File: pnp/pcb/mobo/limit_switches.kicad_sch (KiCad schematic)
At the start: 6 parts, among them J2 X_LIMIT, J3 Y_LIMIT, J4 Z_LIMIT, J5 L_LIMIT, J6 R_LIMIT, J7 A_LIMIT

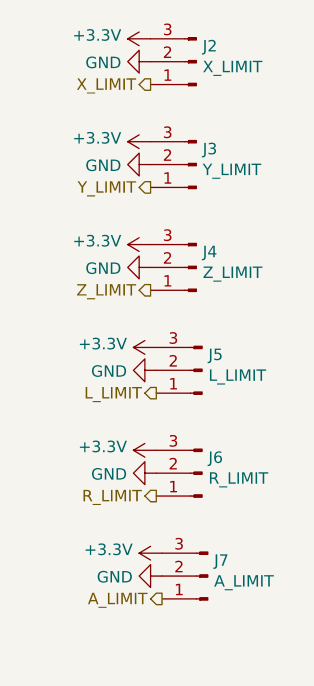
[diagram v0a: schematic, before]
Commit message: All sheets cleaned up
All symbols and their fields are now neatly organized.

All hierarchical pins are already imported,
except for the microcontroller sheet.
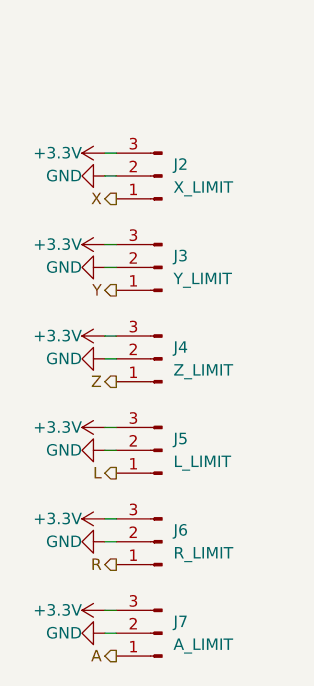
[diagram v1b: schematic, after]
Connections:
- net A_LIMIT renamed A
- net L_LIMIT renamed L
- net R_LIMIT renamed R
- net X_LIMIT renamed X
- net Y_LIMIT renamed Y
- net Z_LIMIT renamed Z
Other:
- moved on the sheet: J2, J3, J4, J5, J6, J7

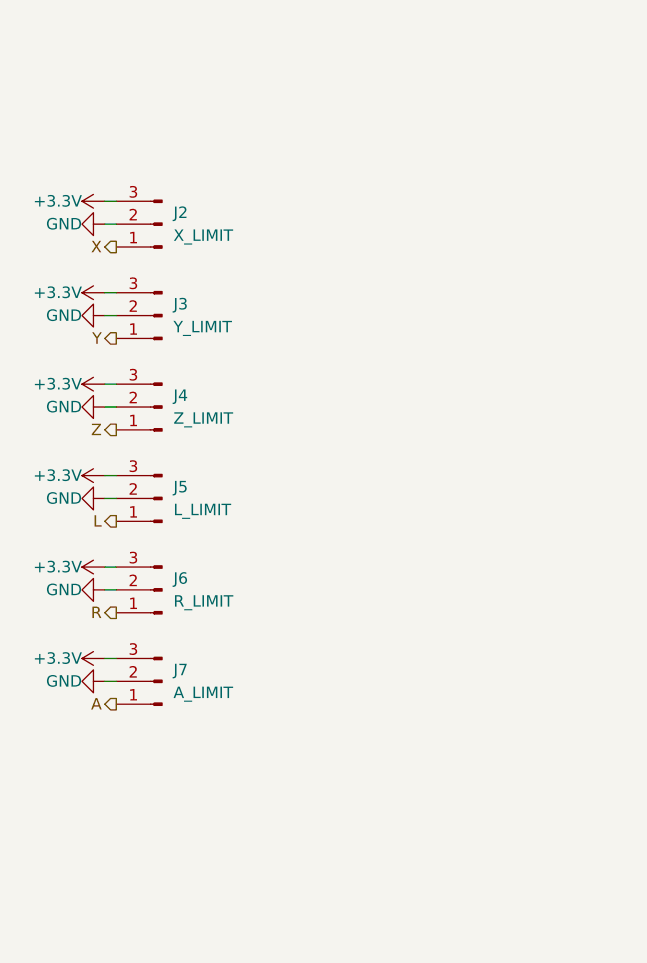
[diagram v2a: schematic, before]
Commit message: moving mobo-rev04b0 into mobo-rev04 branch from old repo
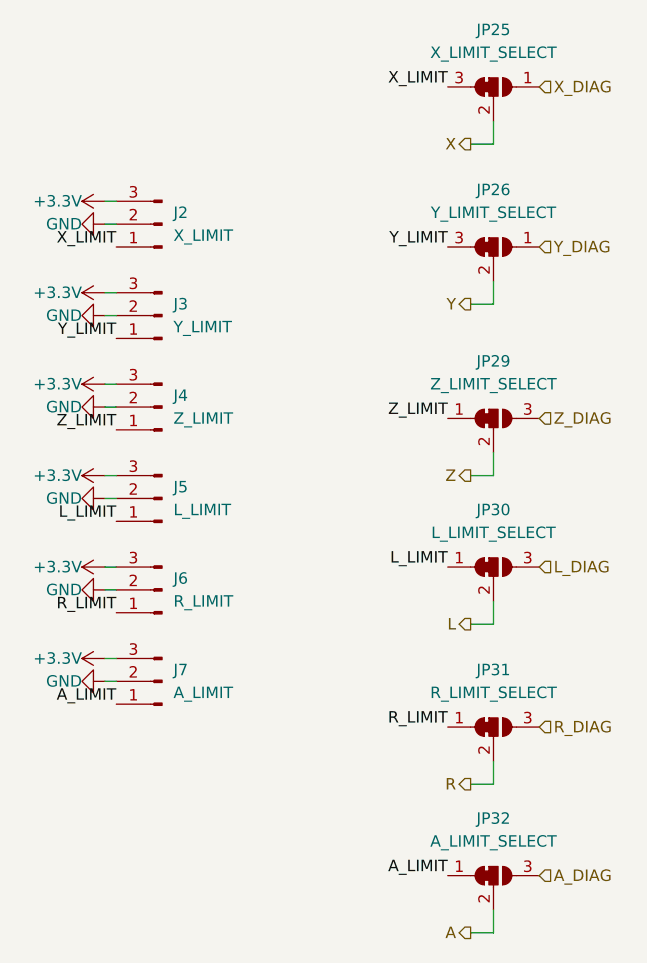
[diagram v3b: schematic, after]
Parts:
- added JP25: X_LIMIT_SELECT, Jumper:SolderJumper-3_P1.3mm_Bridged12_RoundedPad1.0x1.5mm, symbol index:SolderJumper_3_Bridged23
- added JP26: Y_LIMIT_SELECT, Jumper:SolderJumper-3_P1.3mm_Bridged12_RoundedPad1.0x1.5mm, symbol index:SolderJumper_3_Bridged23
- added JP29: Z_LIMIT_SELECT, Jumper:SolderJumper-3_P1.3mm_Bridged12_RoundedPad1.0x1.5mm, symbol Jumper:SolderJumper_3_Bridged12
- added JP30: L_LIMIT_SELECT, Jumper:SolderJumper-3_P1.3mm_Bridged12_RoundedPad1.0x1.5mm, symbol Jumper:SolderJumper_3_Bridged12
- added JP31: R_LIMIT_SELECT, Jumper:SolderJumper-3_P1.3mm_Bridged12_RoundedPad1.0x1.5mm, symbol Jumper:SolderJumper_3_Bridged12
- added JP32: A_LIMIT_SELECT, Jumper:SolderJumper-3_P1.3mm_Bridged12_RoundedPad1.0x1.5mm, symbol Jumper:SolderJumper_3_Bridged12
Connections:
- net A: now also JP32.2 (C); no longer J7.1 (Pin_1)
- net L: now also JP30.2 (C); no longer J5.1 (Pin_1)
- net R: now also JP31.2 (C); no longer J6.1 (Pin_1)
- net X: now also JP25.2 (C); no longer J2.1 (Pin_1)
- net Y: now also JP26.2 (C); no longer J3.1 (Pin_1)
- net Z: now also JP29.2 (C); no longer J4.1 (Pin_1)
- new net A_DIAG: JP32.3 (B)
- new net A_LIMIT: J7.1 (Pin_1), JP32.1 (A)
- new net L_DIAG: JP30.3 (B)
- new net L_LIMIT: J5.1 (Pin_1), JP30.1 (A)
- new net R_DIAG: JP31.3 (B)
- new net R_LIMIT: J6.1 (Pin_1), JP31.1 (A)
- new net X_DIAG: JP25.1 (B)
- new net X_LIMIT: J2.1 (Pin_1), JP25.3 (A)
- new net Y_DIAG: JP26.1 (B)
- new net Y_LIMIT: J3.1 (Pin_1), JP26.3 (A)
- new net Z_DIAG: JP29.3 (B)
- new net Z_LIMIT: J4.1 (Pin_1), JP29.1 (A)
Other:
- company: (none) -> Opulo
- title: (none) -> LumenPnP Motherboard
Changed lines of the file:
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@@
   (paper "A4")
   (title_block
+    (title "LumenPnP Motherboard")
     (date "2022-03-29")
+    (company "Opulo")
   )
   (wire (pts (xy 146.05 83.82) (xy 147.32 83.82))
@@
     (stroke (width 0) (type default) (color 0 0 0 0))
   )
+  (wire (pts (xy 189.23 111.76) (xy 189.23 109.22))
+    (stroke (width 0) (type default) (color 0 0 0 0))
+  )
+  (wire (pts (xy 189.23 146.05) (xy 189.23 143.51))
+    (stroke (width 0) (type default) (color 0 0 0 0))
+  )
+  (wire (pts (xy 186.69 74.93) (xy 189.23 74.93))
+    (stroke (width 0) (type default) (color 0 0 0 0))
+  )
   (wire (pts (xy 146.05 104.14) (xy 147.32 104.14))
     (stroke (width 0) (type default) (color 0 0 0 0))
   )
+  (wire (pts (xy 189.23 162.56) (xy 189.23 160.02))
+    (stroke (width 0) (type default) (color 0 0 0 0))
+  )
+  (wire (pts (xy 186.69 128.27) (xy 189.23 128.27))
+    (stroke (width 0) (type default) (color 0 0 0 0))
+  )
   (wire (pts (xy 146.05 114.3) (xy 147.32 114.3))
     (stroke (width 0) (type default) (color 0 0 0 0))
   )
+  (wire (pts (xy 189.23 74.93) (xy 189.23 72.39))
+    (stroke (width 0) (type default) (color 0 0 0 0))
+  )
   (wire (pts (xy 146.05 111.76) (xy 147.32 111.76))
     (stroke (width 0) (type default) (color 0 0 0 0))
   )
+  (wire (pts (xy 186.69 92.71) (xy 189.23 92.71))
+    (stroke (width 0) (type default) (color 0 0 0 0))
+  )
   (wire (pts (xy 146.05 121.92) (xy 147.32 121.92))
     (stroke (width 0) (type default) (color 0 0 0 0))
   )
+  (wire (pts (xy 186.69 146.05) (xy 189.23 146.05))
+    (stroke (width 0) (type default) (color 0 0 0 0))
+  )
+  (wire (pts (xy 186.69 162.56) (xy 189.23 162.56))
+    (stroke (width 0) (type default) (color 0 0 0 0))
+  )
   (wire (pts (xy 146.05 93.98) (xy 147.32 93.98))
     (stroke (width 0) (type default) (color 0 0 0 0))
   )
+  (wire (pts (xy 186.69 111.76) (xy 189.23 111.76))
+    (stroke (width 0) (type default) (color 0 0 0 0))
+  )
   (wire (pts (xy 146.05 81.28) (xy 147.32 81.28))
     (stroke (width 0) (type default) (color 0 0 0 0))
   )
+  (wire (pts (xy 189.23 92.71) (xy 189.23 90.17))
+    (stroke (width 0) (type default) (color 0 0 0 0))
+  )
   (wire (pts (xy 146.05 124.46) (xy 147.32 124.46))
     (stroke (width 0) (type default) (color 0 0 0 0))
@@
     (stroke (width 0) (type default) (color 0 0 0 0))
   )
-  (hierarchical_label "X" (shape output) (at 147.32 86.36 180)
+  (wire (pts (xy 189.23 128.27) (xy 189.23 125.73))
+    (stroke (width 0) (type default) (color 0 0 0 0))
+  )
+  (label "X_LIMIT" (at 147.32 86.36 180)
+    (effects (font (size 1.27 1.27)) (justify right bottom))
+  )
+  (label "Y_LIMIT" (at 147.32 96.52 180)
+    (effects (font (size 1.27 1.27)) (justify right bottom))
+  )
+  (label "R_LIMIT" (at 184.15 139.7 180)
+    (effects (font (size 1.27 1.27)) (justify right bottom))
+  )
+  (label "R_LIMIT" (at 147.32 127 180)
+    (effects (font (size 1.27 1.27)) (justify right bottom))
+  )
+  (label "X_LIMIT" (at 184.15 68.58 180)
+    (effects (font (size 1.27 1.27)) (justify right bottom))
+  )
+  (label "L_LIMIT" (at 184.15 121.92 180)
+    (effects (font (size 1.27 1.27)) (justify right bottom))
+  )
+  (label "Z_LIMIT" (at 184.15 105.41 180)
+    (effects (font (size 1.27 1.27)) (justify right bottom))
+  )
+  (label "Y_LIMIT" (at 184.15 86.36 180)
+    (effects (font (size 1.27 1.27)) (justify right bottom))
+  )
+  (label "A_LIMIT" (at 147.32 137.16 180)
+    (effects (font (size 1.27 1.27)) (justify right bottom))
+  )
+  (label "A_LIMIT" (at 184.15 156.21 180)
+    (effects (font (size 1.27 1.27)) (justify right bottom))
+  )
+  (label "Z_LIMIT" (at 147.32 106.68 180)
+    (effects (font (size 1.27 1.27)) (justify right bottom))
+  )
+  (label "L_LIMIT" (at 147.32 116.84 180)
+    (effects (font (size 1.27 1.27)) (justify right bottom))
+  )
+  (hierarchical_label "R" (shape output) (at 186.69 146.05 180)
     (effects (font (size 1.27 1.27)) (justify right))
   )
-  (hierarchical_label "R" (shape output) (at 147.32 127 180)
+  (hierarchical_label "X" (shape output) (at 186.69 74.93 180)
     (effects (font (size 1.27 1.27)) (justify right))
   )
-  (hierarchical_label "A" (shape output) (at 147.32 137.16 180)
+  (hierarchical_label "Y" (shape output) (at 186.69 92.71 180)
     (effects (font (size 1.27 1.27)) (justify right))
   )
-  (hierarchical_label "Z" (shape output) (at 147.32 106.68 180)
+  (hierarchical_label "L_DIAG" (shape input) (at 194.31 121.92 0)
+    (effects (font (size 1.27 1.27)) (justify left))
+  )
+  (hierarchical_label "A_DIAG" (shape input) (at 194.31 156.21 0)
+    (effects (font (size 1.27 1.27)) (justify left))
+  )
+  (hierarchical_label "R_DIAG" (shape input) (at 194.31 139.7 0)
+    (effects (font (size 1.27 1.27)) (justify left))
+  )
+  (hierarchical_label "Z" (shape output) (at 186.69 111.76 180)
     (effects (font (size 1.27 1.27)) (justify right))
   )
-  (hierarchical_label "L" (shape output) (at 147.32 116.84 180)
+  (hierarchical_label "A" (shape output) (at 186.69 162.56 180)
     (effects (font (size 1.27 1.27)) (justify right))
   )
-  (hierarchical_label "Y" (shape output) (at 147.32 96.52 180)
+  (hierarchical_label "Y_DIAG" (shape input) (at 194.31 86.36 0)
+    (effects (font (size 1.27 1.27)) (justify left))
+  )
+  (hierarchical_label "L" (shape output) (at 186.69 128.27 180)
     (effects (font (size 1.27 1.27)) (justify right))
+  )
+  (hierarchical_label "X_DIAG" (shape input) (at 194.31 68.58 0)
+    (effects (font (size 1.27 1.27)) (justify left))
+  )
+  (hierarchical_label "Z_DIAG" (shape input) (at 194.31 105.41 0)
+    (effects (font (size 1.27 1.27)) (justify left))
   )
   (symbol (lib_id "power:+3.3V") (at 146.05 132.08 90) (unit 1)
@@
     (pin "1")
   )
+  (symbol (lib_id "index:SolderJumper_3_Bridged23") (at 189.23 86.36 0) (unit 1)
+    (in_bom yes) (on_board yes)
+    (property "Reference" "JP26" (id 0) (at 189.23 80.01 0))
+    (property "Value" "Y_LIMIT_SELECT" (id 1) (at 189.23 82.55 0))
+    (property "Footprint" "Jumper:SolderJumper-3_P1.3mm_Bridged12_RoundedPad1.0x1.5mm" (id 2) (at 189.23 86.36 0)
+      (effects (font (size 1.27 1.27)) hide)
+    )
+    (property "Datasheet" "~" (id 3) (at 189.23 86.36 0)
+      (effects (font (size 1.27 1.27)) hide)
+    )
+    (pin "1")
+    (pin "2")
+    (pin "3")
+  )
   (symbol (lib_id "power:+3.3V") (at 146.05 111.76 90) (unit 1)
     (in_bom yes) (on_board yes)
@@
     (pin "1")
   )
+  (symbol (lib_id "Jumper:SolderJumper_3_Bridged12") (at 189.23 121.92 0) (unit 1)
+    (in_bom yes) (on_board yes)
+    (property "Reference" "JP30" (id 0) (at 189.23 115.57 0))
+    (property "Value" "L_LIMIT_SELECT" (id 1) (at 189.23 118.11 0))
+    (property "Footprint" "Jumper:SolderJumper-3_P1.3mm_Bridged12_RoundedPad1.0x1.5mm" (id 2) (at 189.23 121.92 0)
+      (effects (font (size 1.27 1.27)) hide)
+    )
+    (property "Datasheet" "~" (id 3) (at 189.23 121.92 0)
+      (effects (font (size 1.27 1.27)) hide)
+    )
+    (pin "1")
+    (pin "2")
+    (pin "3")
+  )
   (symbol (lib_id "power:+3.3V") (at 146.05 101.6 90) (unit 1)
     (in_bom yes) (on_board yes)
@@
     (pin "1")
   )
+  (symbol (lib_id "index:SolderJumper_3_Bridged23") (at 189.23 68.58 0) (unit 1)
+    (in_bom yes) (on_board yes)
+    (property "Reference" "JP25" (id 0) (at 189.23 62.23 0))
+    (property "Value" "X_LIMIT_SELECT" (id 1) (at 189.23 64.77 0))
+    (property "Footprint" "Jumper:SolderJumper-3_P1.3mm_Bridged12_RoundedPad1.0x1.5mm" (id 2) (at 189.23 68.58 0)
+      (effects (font (size 1.27 1.27)) hide)
+    )
+    (property "Datasheet" "~" (id 3) (at 189.23 68.58 0)
+      (effects (font (size 1.27 1.27)) hide)
+    )
+    (pin "1")
+    (pin "2")
+    (pin "3")
+  )
   (symbol (lib_id "power:GND") (at 146.05 114.3 270) (unit 1)
     (in_bom yes) (on_board yes)
@@
     (pin "1")
   )
+  (symbol (lib_id "Jumper:SolderJumper_3_Bridged12") (at 189.23 105.41 0) (unit 1)
+    (in_bom yes) (on_board yes)
+    (property "Reference" "JP29" (id 0) (at 189.23 99.06 0))
+    (property "Value" "Z_LIMIT_SELECT" (id 1) (at 189.23 101.6 0))
+    (property "Footprint" "Jumper:SolderJumper-3_P1.3mm_Bridged12_RoundedPad1.0x1.5mm" (id 2) (at 189.23 105.41 0)
+      (effects (font (size 1.27 1.27)) hide)
+    )
+    (property "Datasheet" "~" (id 3) (at 189.23 105.41 0)
+      (effects (font (size 1.27 1.27)) hide)
+    )
+    (pin "1")
+    (pin "2")
+    (pin "3")
+  )
   (symbol (lib_id "Connector:Conn_01x03_Male") (at 152.4 134.62 180) (unit 1)
     (in_bom yes) (on_board yes)
@@
     (pin "1")
   )
+  (symbol (lib_id "Jumper:SolderJumper_3_Bridged12") (at 189.23 156.21 0) (unit 1)
+    (in_bom yes) (on_board yes)
+    (property "Reference" "JP32" (id 0) (at 189.23 149.86 0))
+    (property "Value" "A_LIMIT_SELECT" (id 1) (at 189.23 152.4 0))
+    (property "Footprint" "Jumper:SolderJumper-3_P1.3mm_Bridged12_RoundedPad1.0x1.5mm" (id 2) (at 189.23 156.21 0)
+      (effects (font (size 1.27 1.27)) hide)
+    )
+    (property "Datasheet" "~" (id 3) (at 189.23 156.21 0)
+      (effects (font (size 1.27 1.27)) hide)
+    )
+    (pin "1")
+    (pin "2")
+    (pin "3")
+  )
   (symbol (lib_id "Connector:Conn_01x03_Male") (at 152.4 104.14 180) (unit 1)
     (in_bom yes) (on_board yes)
@@
       (effects (font (size 1.27 1.27)) hide)
     )
+    (pin "1")
+    (pin "2")
+    (pin "3")
+  )
+  (symbol (lib_id "Jumper:SolderJumper_3_Bridged12") (at 189.23 139.7 0) (unit 1)
+    (in_bom yes) (on_board yes)
+    (property "Reference" "JP31" (id 0) (at 189.23 133.35 0))
+    (property "Value" "R_LIMIT_SELECT" (id 1) (at 189.23 135.89 0))
+    (property "Footprint" "Jumper:SolderJumper-3_P1.3mm_Bridged12_RoundedPad1.0x1.5mm" (id 2) (at 189.23 139.7 0)
+      (effects (font (size 1.27 1.27)) hide)
+    )
+    (property "Datasheet" "~" (id 3) (at 189.23 139.7 0)
+      (effects (font (size 1.27 1.27)) hide)
+    )

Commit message: Update mobo schematic with part numbers and ratings
All parts now have part numbers for at least one reseller or manufacturer along with rating specifications.

Note: I did not update the PCB with these new properties, as it seems the PCB is a bit out of sync with the schematic.
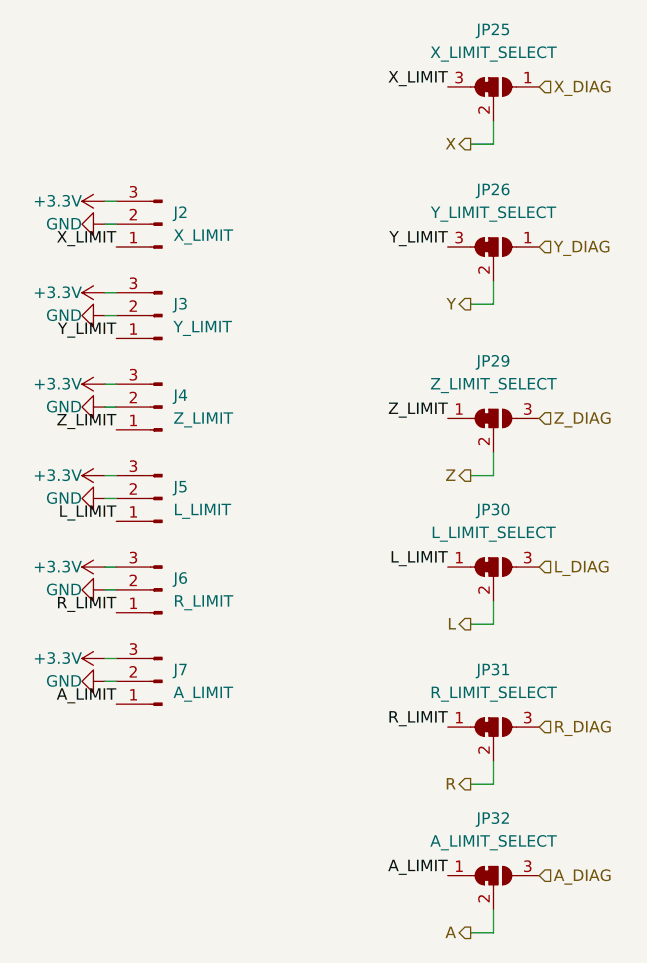
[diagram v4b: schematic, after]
